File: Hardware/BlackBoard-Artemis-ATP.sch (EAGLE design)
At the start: 83 parts, among them IC3 LM1117, J2 CORTEX_DEBUG, J3 POWER_JACKTOE, J5 USB-C, Q1 1.1A/60V/600mΩ, U3 AP2112-3.3V, U4 ARTEMIS_MODULESMD, U5 CH340C, Y1 32.768kHz

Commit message: Fixes from design review. Route away from antenna.
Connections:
- net ~AD3/SWO renamed ~AD33/SWO
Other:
- moved on the sheet: C11, C13, J2, J6, JP21, JP22, TP1, TP2, TP3, U4, Y1

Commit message: Moved SWDIO test point. Removed TP5/6.
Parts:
- removed TP5, TP6: TEST-POINT3X5, SparkFun-Connectors:TEST-POINT3X5
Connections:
- net RXI-0: no longer TP5.1
- net TXO-0: no longer TP6.1
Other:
- moved on the sheet: J7
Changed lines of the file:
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@@
 <part name="GND8" library="SparkFun-PowerSymbols" deviceset="GND" device=""/>
 <part name="R9" library="SparkFun-Resistors" deviceset="10KOHM" device="-0603-1/10W-1%" value="10k"/>
-<part name="TP5" library="SparkFun-Connectors" deviceset="TEST-POINT" device="3X5"/>
-<part name="TP6" library="SparkFun-Connectors" deviceset="TEST-POINT" device="3X5"/>
 <part name="C1" library="SparkFun-Capacitors" deviceset="2.2UF" device="-0603-10V-20%" value="2.2uF"/>
 <part name="C7" library="SparkFun-Capacitors" deviceset="10UF" device="-0603-6.3V-20%" value="10uF"/>
@@
 <attribute name="VALUE" x="23.876" y="129.54" size="1.778" layer="96" font="vector" rot="MR90" align="top-center"/>
 </instance>
-<instance part="TP5" gate="G$1" x="134.62" y="30.48" smashed="yes">
-<attribute name="NAME" x="134.62" y="31.496" size="1.778" layer="95" font="vector"/>
-</instance>
-<instance part="TP6" gate="G$1" x="134.62" y="25.4" smashed="yes">
-<attribute name="NAME" x="134.62" y="26.416" size="1.778" layer="95" font="vector"/>
-</instance>
 <instance part="C1" gate="G$1" x="20.32" y="137.16" smashed="yes" rot="R90">
 <attribute name="NAME" x="17.399" y="138.684" size="1.778" layer="95" font="vector" rot="R90"/>
@@
 <attribute name="VALUE" x="45.72" y="119.126" size="1.778" layer="96" align="top-center"/>
 </instance>
-<instance part="J7" gate="G$1" x="139.7" y="17.78" smashed="yes" rot="R180">
-<attribute name="VALUE" x="142.24" y="22.606" size="1.778" layer="96" font="vector" rot="R180"/>
-<attribute name="NAME" x="142.24" y="12.192" size="1.778" layer="95" font="vector" rot="R180"/>
+<instance part="J7" gate="G$1" x="139.7" y="30.48" smashed="yes" rot="R180">
+<attribute name="VALUE" x="142.24" y="35.306" size="1.778" layer="96" font="vector" rot="R180"/>
+<attribute name="NAME" x="142.24" y="24.892" size="1.778" layer="95" font="vector" rot="R180"/>
 </instance>
 <instance part="C28" gate="G$1" x="30.48" y="83.82" smashed="yes" rot="MR0">
@@
 <wire x1="129.54" y1="40.64" x2="129.54" y2="38.1" width="0.1524" layer="91"/>
 <junction x="129.54" y="38.1"/>
-<pinref part="TP5" gate="G$1" pin="1"/>
-<wire x1="134.62" y1="30.48" x2="129.54" y2="30.48" width="0.1524" layer="91"/>
-<wire x1="129.54" y1="30.48" x2="129.54" y2="38.1" width="0.1524" layer="91"/>
-<wire x1="129.54" y1="30.48" x2="129.54" y2="17.78" width="0.1524" layer="91"/>
-<junction x="129.54" y="30.48"/>
+<wire x1="129.54" y1="38.1" x2="129.54" y2="30.48" width="0.1524" layer="91"/>
 <pinref part="J7" gate="G$1" pin="1"/>
-<wire x1="129.54" y1="17.78" x2="132.08" y2="17.78" width="0.1524" layer="91"/>
+<wire x1="129.54" y1="30.48" x2="132.08" y2="30.48" width="0.1524" layer="91"/>
 </segment>
 <segment>
@@
 <wire x1="119.38" y1="40.64" x2="119.38" y2="35.56" width="0.1524" layer="91"/>
 <junction x="119.38" y="35.56"/>
-<pinref part="TP6" gate="G$1" pin="1"/>
-<wire x1="134.62" y1="25.4" x2="127" y2="25.4" width="0.1524" layer="91"/>
-<wire x1="127" y1="25.4" x2="127" y2="35.56" width="0.1524" layer="91"/>
 <junction x="127" y="35.56"/>
-<wire x1="127" y1="25.4" x2="127" y2="15.24" width="0.1524" layer="91"/>
-<junction x="127" y="25.4"/>
+<wire x1="127" y1="35.56" x2="127" y2="27.94" width="0.1524" layer="91"/>
 <pinref part="J7" gate="G$1" pin="2"/>
-<wire x1="127" y1="15.24" x2="132.08" y2="15.24" width="0.1524" layer="91"/>
+<wire x1="127" y1="27.94" x2="132.08" y2="27.94" width="0.1524" layer="91"/>
 </segment>
 <segment>

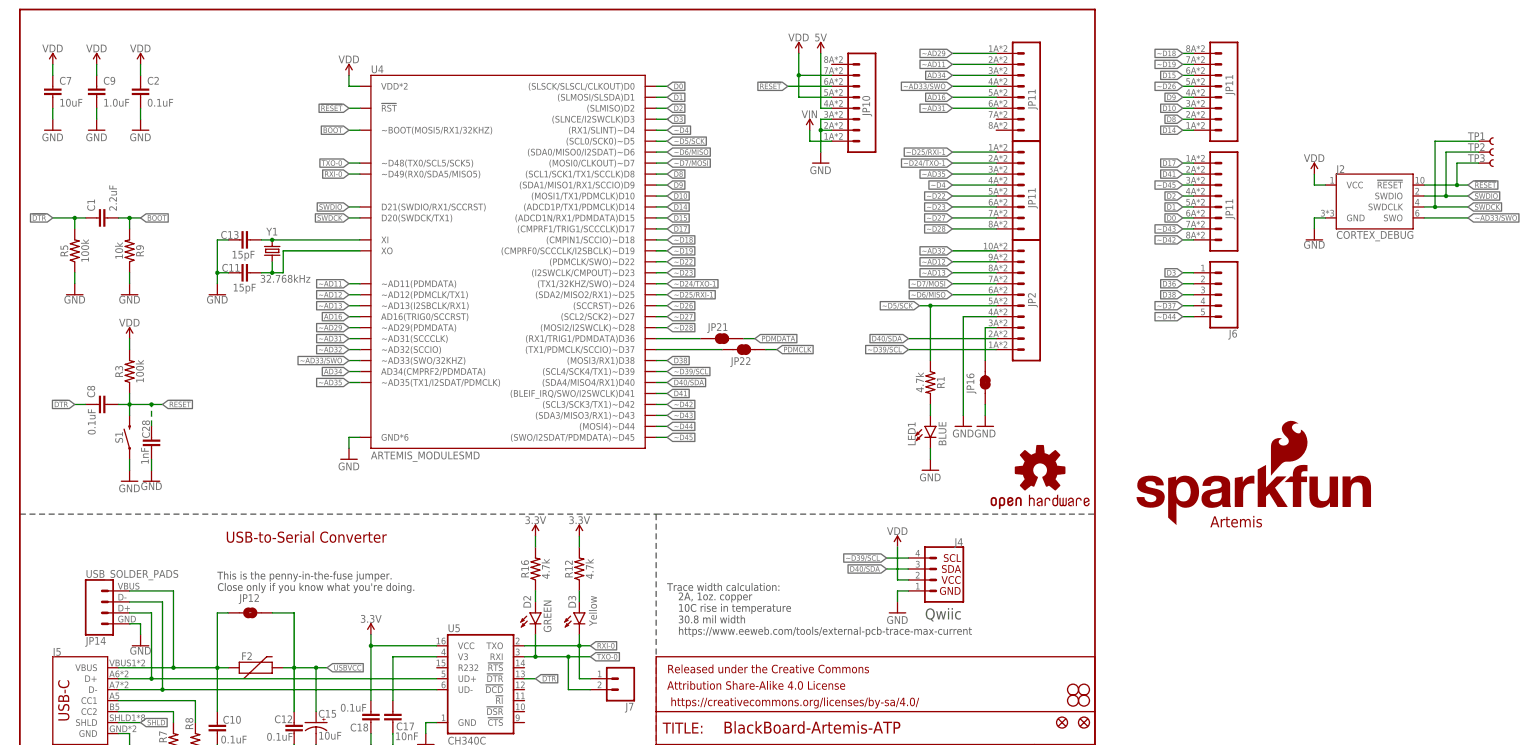
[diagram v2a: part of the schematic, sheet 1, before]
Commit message: Move TP for easier testing. Remove TP on serial. Adjust sch blocks.
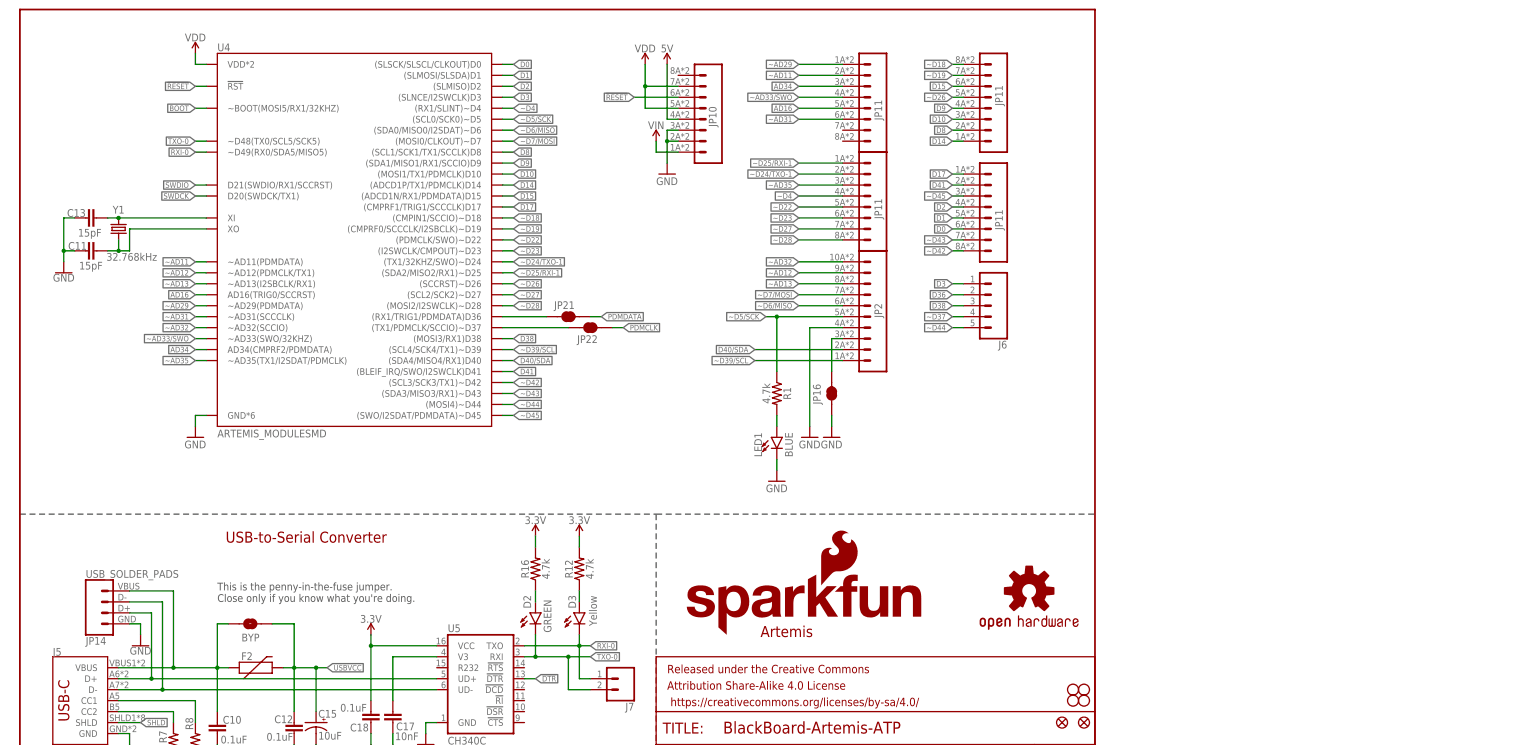
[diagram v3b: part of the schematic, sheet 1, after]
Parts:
- removed JP12: JUMPER-SMT_2_NO_SILK, SparkFun-Jumpers:JUMPER-SMT_2_NO_SILK
- added BYP: BYP, SparkFun-Jumpers:JUMPER-SMT_2_NO_SILK
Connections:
- net USBVCC: now also BYP.2; no longer JP12.2
- net VUSB: now also BYP.1; no longer JP12.1
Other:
- note added: "Artemis Decoupling"
- note added: "Bootload Reset Circuit"
- note added: "JTAG"
- moved on the sheet: BT1, C11, C13, C16, C19, C3, C4, C5, C6, D1, D4, D5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
